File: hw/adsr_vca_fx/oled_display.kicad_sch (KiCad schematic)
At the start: 1 part, among them J5 Conn_01x04

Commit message: added OLED footprint
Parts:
- J5: footprint Connector_PinHeader_2.54mm:PinHeader_1x04_P2.54mm_Vertical -> 128x64_0_96InchOLED:128x64_0_96InchOLED
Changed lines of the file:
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@@
       (effects (font (size 1.27 1.27)) (justify left))
     )
-    (property "Footprint" "Connector_PinHeader_2.54mm:PinHeader_1x04_P2.54mm_Vertical" (at 208.28 91.44 0)
+    (property "Footprint" "128x64_0_96InchOLED:128x64_0_96InchOLED" (at 208.28 91.44 0)
       (effects (font (size 1.27 1.27)) hide)
     )

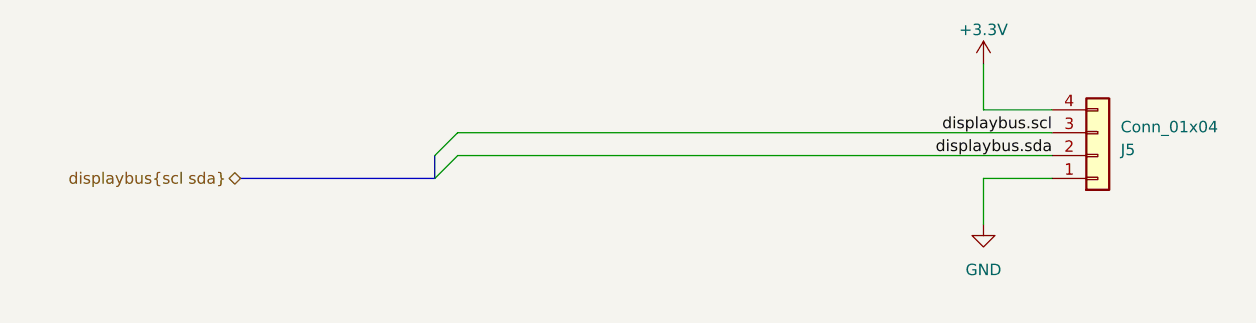
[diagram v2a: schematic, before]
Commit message: updated layout
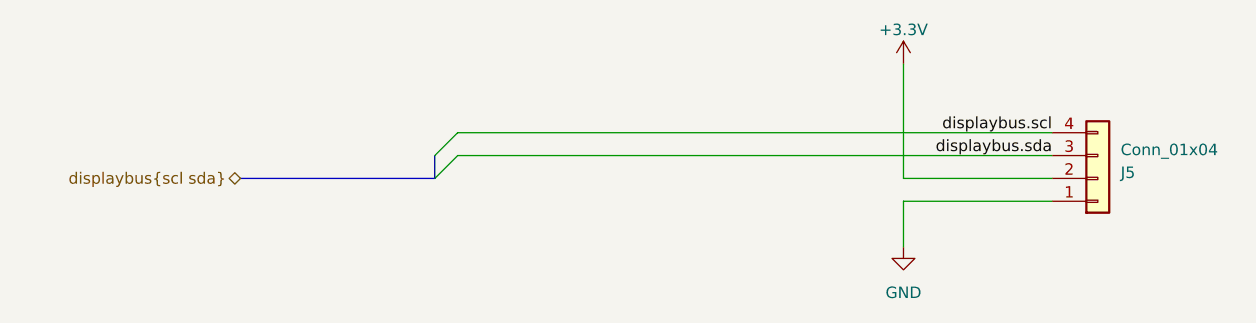
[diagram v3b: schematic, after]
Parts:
- J5: footprint 128x64_0_96InchOLED:128x64_0_96InchOLED -> SSD1306_0.96_Oled:SSD1306_0.96_Oled_no_courtyard_no_silkscreen
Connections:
- net +3.3V: now also J5.2 (Pin_2); no longer J5.4 (Pin_4)
- net displaybus.scl: now also J5.4 (Pin_4); no longer J5.3 (Pin_3)
- net displaybus.sda: now also J5.3 (Pin_3); no longer J5.2 (Pin_2)
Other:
- moved on the sheet: J5
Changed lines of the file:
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@@
+    (stroke (width 0) (type default))
+  )
+  (wire (pts (xy 137.16 88.9) (xy 203.2 88.9))
     (stroke (width 0) (type default))
   )
@@
     (stroke (width 0) (type default))
   )
-  (wire (pts (xy 203.2 93.98) (xy 195.58 93.98))
+  (wire (pts (xy 186.69 96.52) (xy 203.2 96.52))
     (stroke (width 0) (type default))
   )
@@
     (stroke (width 0) (type default))
   )
-  (wire (pts (xy 203.2 88.9) (xy 137.16 88.9))
+  (wire (pts (xy 203.2 93.98) (xy 186.69 93.98))
     (stroke (width 0) (type default))
   )
-  (wire (pts (xy 203.2 86.36) (xy 195.58 86.36))
-    (stroke (width 0) (type default))
-  )
-  (wire (pts (xy 195.58 81.28) (xy 195.58 86.36))
+  (wire (pts (xy 186.69 81.28) (xy 186.69 93.98))
     (stroke (width 0) (type default))
   )
@@
     (stroke (width 0) (type default))
   )
-  (wire (pts (xy 195.58 93.98) (xy 195.58 99.06))
+  (wire (pts (xy 186.69 96.52) (xy 186.69 101.6))
     (stroke (width 0) (type default))
   )
@@
     (effects (font (size 1.27 1.27)) (justify right))
   )
-  (symbol (lib_id "power:+3.3V") (at 195.58 81.28 0) (unit 1)
+  (symbol (lib_id "power:+3.3V") (at 186.69 81.28 0) (unit 1)
     (in_bom yes) (on_board yes) (dnp no) (fields_autoplaced)
-    (property "Reference" "#PWR038" (at 195.58 85.09 0)
+    (property "Reference" "#PWR038" (at 186.69 85.09 0)
       (effects (font (size 1.27 1.27)) hide)
     )
-    (property "Value" "+3.3V" (at 195.58 77.47 0)
+    (property "Value" "+3.3V" (at 186.69 77.47 0)
       (effects (font (size 1.27 1.27)))
     )
-    (property "Footprint" "" (at 195.58 81.28 0)
+    (property "Footprint" "" (at 186.69 81.28 0)
       (effects (font (size 1.27 1.27)) hide)
     )
-    (property "Datasheet" "" (at 195.58 81.28 0)
+    (property "Datasheet" "" (at 186.69 81.28 0)
       (effects (font (size 1.27 1.27)) hide)
     )
@@
     )
   )
-  (symbol (lib_id "Connector_Generic:Conn_01x04") (at 208.28 91.44 0) (mirror x) (unit 1)
+  (symbol (lib_id "Connector_Generic:Conn_01x04") (at 208.28 93.98 0) (mirror x) (unit 1)
     (in_bom yes) (on_board yes) (dnp no)
-    (property "Reference" "J5" (at 210.82 90.805 0)
+    (property "Reference" "J5" (at 210.82 93.345 0)
       (effects (font (size 1.27 1.27)) (justify left))
     )
-    (property "Value" "Conn_01x04" (at 210.82 88.265 0)
+    (property "Value" "Conn_01x04" (at 210.82 90.805 0)
       (effects (font (size 1.27 1.27)) (justify left))
     )
-    (property "Footprint" "128x64_0_96InchOLED:128x64_0_96InchOLED" (at 208.28 91.44 0)
+    (property "Footprint" "SSD1306_0.96_Oled:SSD1306_0.96_Oled_no_courtyard_no_silkscreen" (at 208.28 93.98 0)
       (effects (font (size 1.27 1.27)) hide)
     )
-    (property "Datasheet" "~" (at 208.28 91.44 0)
+    (property "Datasheet" "~" (at 208.28 93.98 0)
       (effects (font (size 1.27 1.27)) hide)
     )
@@
     )
   )
-  (symbol (lib_id "power:GND") (at 195.58 99.06 0) (unit 1)
+  (symbol (lib_id "power:GND") (at 186.69 101.6 0) (unit 1)
     (in_bom yes) (on_board yes) (dnp no) (fields_autoplaced)
-    (property "Reference" "#PWR039" (at 195.58 105.41 0)
+    (property "Reference" "#PWR039" (at 186.69 107.95 0)
       (effects (font (size 1.27 1.27)) hide)
     )
-    (property "Value" "GND" (at 195.58 104.14 0)
+    (property "Value" "GND" (at 186.69 106.68 0)
       (effects (font (size 1.27 1.27)))
     )
-    (property "Footprint" "" (at 195.58 99.06 0)
+    (property "Footprint" "" (at 186.69 101.6 0)
       (effects (font (size 1.27 1.27)) hide)
     )
-    (property "Datasheet" "" (at 195.58 99.06 0)
+    (property "Datasheet" "" (at 186.69 101.6 0)
       (effects (font (size 1.27 1.27)) hide)
     )
